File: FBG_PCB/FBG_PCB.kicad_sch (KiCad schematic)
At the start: 36 parts, among them J1 Ground, J10 Pont diviseur Echo In 1-4, J11 17V, J12 17V, J13 Echo Out 5-8, J14 17V, J15 Buck converter 17V/5V, J16 Raspberry Power, J17 ES 5V + 5V, J18 5V, J19 5V, J2 Main switch + ES 17V, J20 5V, J21 5V, J3 Ground, J4 Ground, J5 Ground, J6 Echo Out 1-4, J8 Vin 17V, J9 Pont diviseur Echo In 5-8

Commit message: Lot of new connectors
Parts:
- removed J12, J14: 17V, Connector_Molex:Molex_SL_171971-0004_1x04_P2.54mm_Vertical, symbol Connector:Conn_01x04_Pin
- added J19: switch + ES 12V, Connector_Molex:Molex_SL_171971-0004_1x04_P2.54mm_Vertical, symbol Connector:Conn_01x04_Pin
- added J2: Vin 12V, Connector_JST:JST_NV_B02P-NV_1x02_P5.00mm_Vertical, symbol Connector:Conn_01x02_Pin
- added J20, J21: 12V, Connector_Molex:Molex_SL_171971-0004_1x04_P2.54mm_Vertical, symbol Connector:Conn_01x04_Pin
- added J26: Control Driver Motor In, Connector_Molex:Molex_SL_171971-0004_1x04_P2.54mm_Vertical, symbol Connector:Conn_01x04_Pin
- added J27: Control Driver Motor In +Out, Connector_Molex:Molex_SL_171971-0004_1x04_P2.54mm_Vertical, symbol Connector:Conn_01x04_Pin
- added J28: Control Driver Motor Out, Connector_Molex:Molex_SL_171971-0004_1x04_P2.54mm_Vertical, symbol Connector:Conn_01x04_Pin
- added J29, J30, J31, J8, J9: Ground, Connector_Molex:Molex_SL_171971-0004_1x04_P2.54mm_Vertical, symbol Connector:Conn_01x04_Pin
- J10: renamed from J2; value Main switch + ES 17V -> Raspberry +17V switch
- J11: renamed from J15; value Buck converter 17V/5V -> Buck converter 17V/5V
- J12: renamed from J16; value Raspberry Power -> Raspberry Power+ 5V
- renumbered J8 to J1, J11 to J13, J17 to J14, J18 to J15, J19 to J16, J20 to J17, J21 to J18, J10 to J22, J9 to J23, J6 to J24, J13 to J25, J5 to J4, J1 to J5, J3 to J6, J4 to J7, R11 to R10, R13 to R11, R15 to R12, R10 to R13, R12 to R14, R14 to R15, R7 to R4, R4 to R5, R5 to R6, R6 to R7
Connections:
- net at R4.2, R8.1: now also J24.1 (Pin_1); no longer J24.4 (Pin_4)
- net at R11.2, R15.1: now also J25.2 (Pin_2); no longer J25.3 (Pin_3)
- net at J1.2 (Pin_2), J11.3 (Pin_3), J4.1 (Pin_1)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: now also J2.2 (Pin_2), J8.1 (Pin_1), J8.2 (Pin_2), J8.3 (Pin_3), J8.4 (Pin_4), J9.1 (Pin_1), J9.2 (Pin_2), J9.3 (Pin_3), J9.4 (Pin_4)
- net at J10.4 (Pin_4), J13.1 (Pin_1), J13.2 (Pin_2)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: now also J10.2 (Pin_2), J10.3 (Pin_3), J11.4 (Pin_4)
- net at R3.2, R7.1: now also J24.2 (Pin_2); no longer J24.3 (Pin_3)
- net at R10.2, R14.1: now also J25.3 (Pin_3); no longer J25.2 (Pin_2)
- net at R2.2, R6.1: now also J24.3 (Pin_3); no longer J24.2 (Pin_2)
- net at R12.2, R16.1: now also J25.1 (Pin_1); no longer J25.4 (Pin_4)
- net at R1.2, R5.1: now also J24.4 (Pin_4); no longer J24.1 (Pin_1)
- net at R13.1, R9.2: now also J25.4 (Pin_4); no longer J25.1 (Pin_1)
- new net: J19.1 (Pin_1), J20.1 (Pin_1), J20.2 (Pin_2), J20.3 (Pin_3), J20.4 (Pin_4), J21.1 (Pin_1), J21.2 (Pin_2), J21.3 (Pin_3), J21.4 (Pin_4)
- new net: J19.4 (Pin_4), J2.1 (Pin_1)
- new net: J27.1 (Pin_1), J27.4 (Pin_4)
- new net: J27.2 (Pin_2), J27.3 (Pin_3)
- new net: J26.1 (Pin_1), J28.1 (Pin_1)
- new net: J26.2 (Pin_2), J28.2 (Pin_2)
- new net: J26.3 (Pin_3), J28.3 (Pin_3)
- new net: J26.4 (Pin_4), J28.4 (Pin_4)
- new net: J19.2 (Pin_2), J19.3 (Pin_3)
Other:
- moved on the sheet: J1, J14, J15, J16, J17, J18

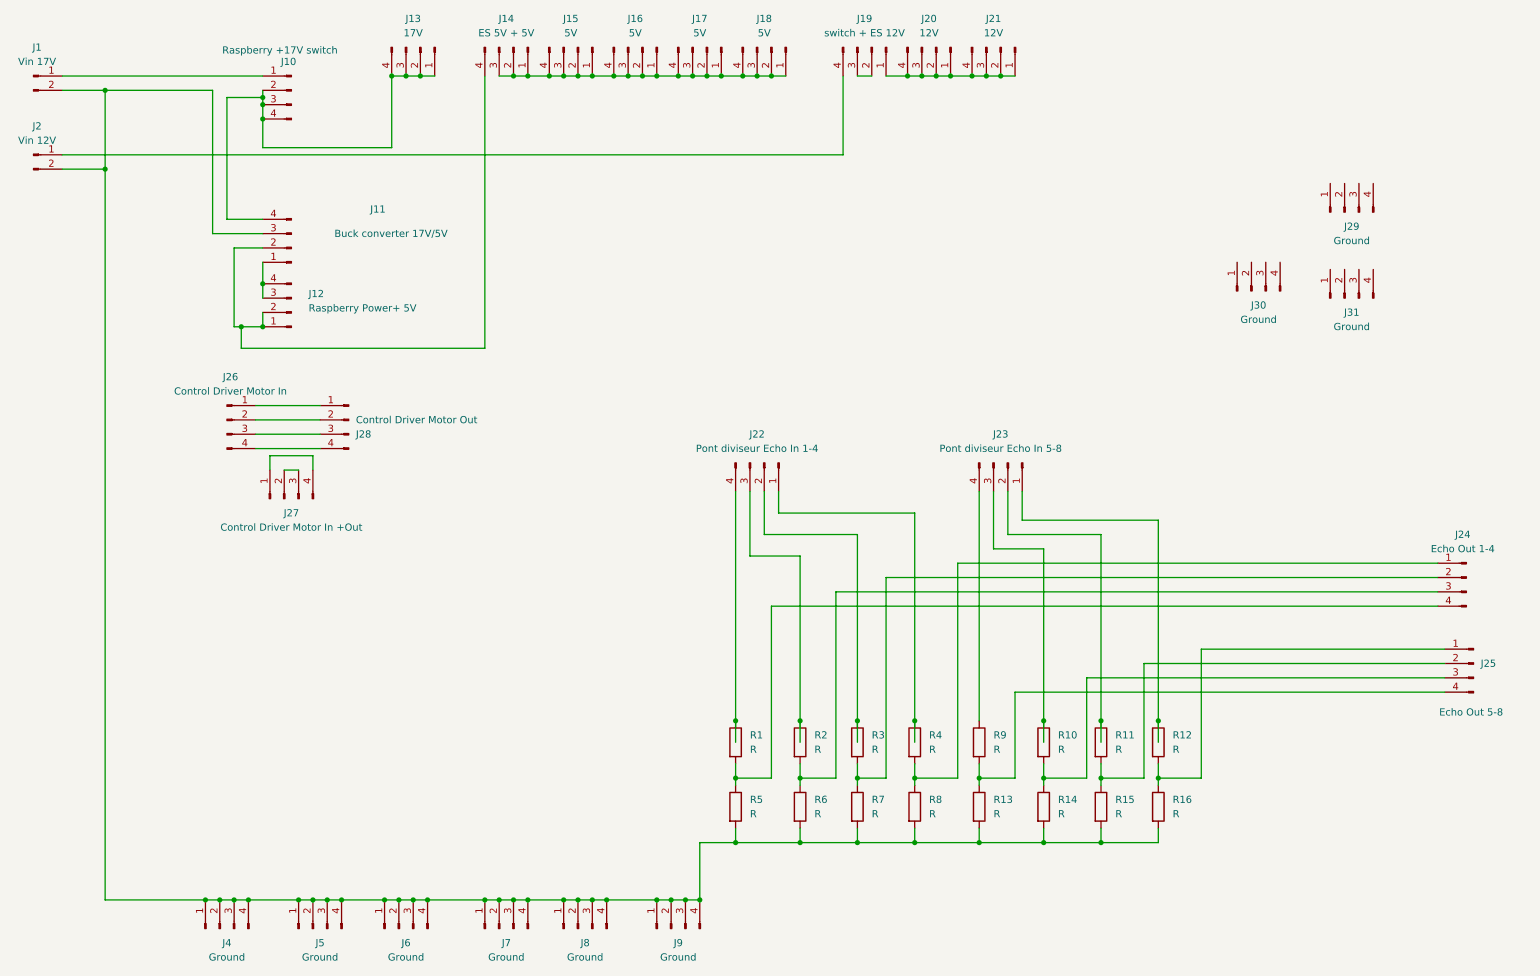
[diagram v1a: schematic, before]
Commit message: trig + echo
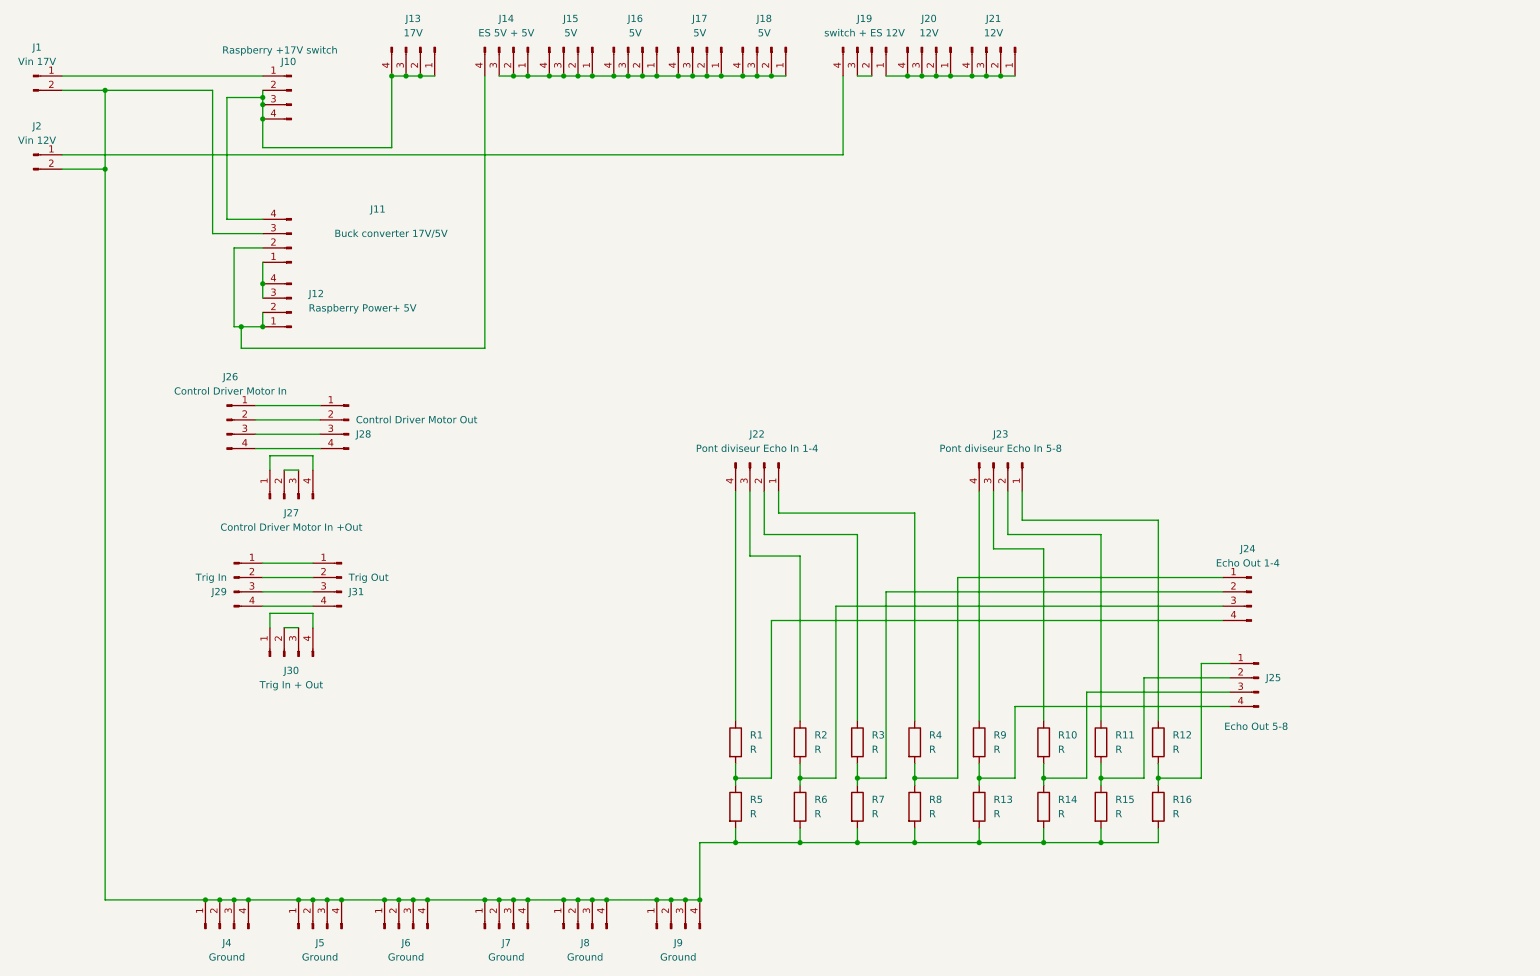
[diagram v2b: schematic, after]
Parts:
- J29: value Ground -> Trig In
- J30: value Ground -> Trig In + Out
- J31: value Ground -> Trig Out
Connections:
- net at J29.1 (Pin_1): now also J31.1 (Pin_1)
- net at J29.2 (Pin_2): now also J31.2 (Pin_2)
- net at J29.3 (Pin_3): now also J31.3 (Pin_3)
- net at J29.4 (Pin_4): now also J31.4 (Pin_4)
- net at J30.1 (Pin_1): now also J30.4 (Pin_4)
- net at J30.2 (Pin_2): now also J30.3 (Pin_3)
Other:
- moved on the sheet: J24, J25, J29, J30, J31

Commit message: V1
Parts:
- added J32: I2C Out, Connector_Molex:Molex_SL_171971-0004_1x04_P2.54mm_Vertical, symbol Connector:Conn_01x04_Pin
- added J33: I2C SCL In, Connector_Molex:Molex_SL_171971-0004_1x04_P2.54mm_Vertical, symbol Connector:Conn_01x04_Pin
- added J34: I2C SCL In +SDA In, Connector_Molex:Molex_SL_171971-0004_1x04_P2.54mm_Vertical, symbol Connector:Conn_01x04_Pin
- added J35: I2C SDA In, Connector_Molex:Molex_SL_171971-0004_1x04_P2.54mm_Vertical, symbol Connector:Conn_01x04_Pin
- added J36: Control Motor CanLift Out +In, Connector_Molex:Molex_SL_171971-0004_1x04_P2.54mm_Vertical, symbol Connector:Conn_01x04_Pin
- added J37: Encoder M1 +M2 Out, Connector_Molex:Molex_SL_171971-0004_1x04_P2.54mm_Vertical, symbol Connector:Conn_01x04_Pin
- added J38: Encoder M1 +M2 In, Connector_Molex:Molex_SL_171971-0004_1x04_P2.54mm_Vertical, symbol Connector:Conn_01x04_Pin
- added J39, J41: Bonus Out, Connector_Molex:Molex_SL_171971-0004_1x04_P2.54mm_Vertical, symbol Connector:Conn_01x04_Pin
- added J40, J42: Bonus In, Connector_Molex:Molex_SL_171971-0004_1x04_P2.54mm_Vertical, symbol Connector:Conn_01x04_Pin
- J22: value Pont diviseur Echo In 1-4 -> Pont diviseur Echo Out 1-4
- J23: value Pont diviseur Echo In 5-8 -> Pont diviseur Echo Out 5-8
- J24: value Echo Out 1-4 -> Echo In 1-4
- J25: value Echo Out 5-8 -> Echo In 5-8
- J26: value Control Driver Motor In -> Control Driver Motor Out
- J27: value Control Driver Motor In +Out -> Control Driver Motor Out + Trig Out
- J28: value Control Driver Motor Out -> Control Driver Motor In
- J30: value Trig In + Out -> Control Driver Motor In + Trig In
- R1, R10, R11, R12, R13, R14, R15, R16, R2, R3, R4, R5, R6, R7, R8, R9: footprint Resistor_THT:R_Axial_DIN0411_L9.9mm_D3.6mm_P25.40mm_Horizontal -> Resistor_THT:R_Axial_DIN0207_L6.3mm_D2.5mm_P10.16mm_Horizontal
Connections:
- net at J22.1 (Pin_1): now also R1.1; no longer R4.1
- net at R4.2, R8.1: now also J24.4 (Pin_4); no longer J24.1 (Pin_1)
- net at J1.2 (Pin_2), J2.2 (Pin_2), J4.1 (Pin_1)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: now also J11.2 (Pin_2); no longer J11.3 (Pin_3)
- net at R11.2, R15.1: now also J25.3 (Pin_3); no longer J25.2 (Pin_2)
- net at J22.2 (Pin_2): now also R2.1; no longer R3.1
- net at J22.3 (Pin_3): now also R3.1; no longer R2.1
- net at J22.4 (Pin_4): now also R4.1; no longer R1.1
- net at R3.2, R7.1: now also J24.3 (Pin_3); no longer J24.2 (Pin_2)
- net at R10.2, R14.1: now also J25.2 (Pin_2); no longer J25.3 (Pin_3)
- net at J30.1 (Pin_1): now also J27.1 (Pin_1); no longer J30.4 (Pin_4)
- net at J30.2 (Pin_2): now also J27.2 (Pin_2); no longer J30.3 (Pin_3)
- net at R2.2, R6.1: now also J24.2 (Pin_2); no longer J24.3 (Pin_3)
- net at J23.3 (Pin_3): now also R11.1; no longer R10.1
- net at J23.2 (Pin_2): now also R10.1; no longer R11.1
- net at J10.2 (Pin_2), J10.3 (Pin_3), J10.4 (Pin_4)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: now also J11.1 (Pin_1); no longer J11.4 (Pin_4)
- net at J27.4 (Pin_4): now also J30.4 (Pin_4); no longer J27.1 (Pin_1)
- net at J27.3 (Pin_3): now also J30.3 (Pin_3); no longer J27.2 (Pin_2)
- net at R12.1: now also J23.4 (Pin_4); no longer J23.1 (Pin_1)
- net at R12.2, R16.1: now also J25.4 (Pin_4); no longer J25.1 (Pin_1)
- net at R1.2, R5.1: now also J24.1 (Pin_1); no longer J24.4 (Pin_4)
- net at J12.1 (Pin_1), J12.2 (Pin_2), J14.4 (Pin_4): now also J11.3 (Pin_3); no longer J11.2 (Pin_2)
- net at J12.3 (Pin_3), J12.4 (Pin_4): now also J11.4 (Pin_4); no longer J11.1 (Pin_1)
- net at R9.1: now also J23.1 (Pin_1); no longer J23.4 (Pin_4)
- net at R13.1, R9.2: now also J25.1 (Pin_1); no longer J25.4 (Pin_4)
- new net: J32.1 (Pin_1), J32.2 (Pin_2), J33.1 (Pin_1), J33.2 (Pin_2), J33.3 (Pin_3), J33.4 (Pin_4), J34.1 (Pin_1), J34.2 (Pin_2)
- new net: J39.1 (Pin_1), J40.1 (Pin_1)
- new net: J39.2 (Pin_2), J40.2 (Pin_2)
- new net: J39.3 (Pin_3), J40.3 (Pin_3)
- new net: J39.4 (Pin_4), J40.4 (Pin_4)
- new net: J32.3 (Pin_3), J32.4 (Pin_4), J34.3 (Pin_3), J34.4 (Pin_4), J35.1 (Pin_1), J35.2 (Pin_2), J35.3 (Pin_3), J35.4 (Pin_4)
- new net: J37.1 (Pin_1), J38.1 (Pin_1)
- new net: J37.2 (Pin_2), J38.2 (Pin_2)
- new net: J37.3 (Pin_3), J38.3 (Pin_3)
- new net: J37.4 (Pin_4), J38.4 (Pin_4)
- new net: J36.1 (Pin_1), J36.3 (Pin_3)
- new net: J36.2 (Pin_2), J36.4 (Pin_4)
- new net: J41.1 (Pin_1), J42.1 (Pin_1)
- new net: J41.2 (Pin_2), J42.2 (Pin_2)
- new net: J41.3 (Pin_3), J42.3 (Pin_3)
- new net: J41.4 (Pin_4), J42.4 (Pin_4)
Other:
- moved on the sheet: J11, J26, J27, J28, J29, J30, J31

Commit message: V2.1
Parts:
- J22: value Pont diviseur Echo Out 1-4 -> Echo Out 1-4
- J23: value Pont diviseur Echo Out 5-8 -> Echo Out 5-8
- J26: value Control Driver Motor Out -> Driver Motor Out
- J27: value Control Driver Motor Out + Trig Out -> Driver Motor Out + Trig Out
- J28: value Control Driver Motor In -> Driver Motor In
- J30: value Control Driver Motor In + Trig In -> Driver Motor In + Trig In
- J36: value Control Motor CanLift Out +In -> Motor CanLift Out +In
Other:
- company: (none) -> Noteris Corporation
- title: (none) -> PCB Board Eurobot FBG Team
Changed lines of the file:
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@@
 	(generator_version "9.0")
 	(paper "A4")
+	(title_block
+		(title "PCB Board Eurobot FBG Team")
+		(date "16/03/2025")
+		(rev "1.0")
+		(company "Noteris Corporation")
+	)
 	(junction
 		(at 109.22 25.4)
@@
 			)
 		)
-		(property "Value" "Pont diviseur Echo Out 1-4"
+		(property "Value" "Echo Out 1-4"
 			(at 146.05 91.44 90)
 			(effects
@@
 			)
 		)
-		(property "Value" "Control Driver Motor In + Trig In"
-			(at 108.204 104.648 0)
+		(property "Value" "Driver Motor In + Trig In"
+			(at 102.87 104.394 0)
 			(effects
 				(font
@@
 			)
 		)
-		(property "Value" "Control Driver Motor Out + Trig Out"
+		(property "Value" "Driver Motor Out + Trig Out"
 			(at 51.054 105.156 0)
 			(effects
@@
 			)
 		)
-		(property "Value" "Control Driver Motor Out"
+		(property "Value" "Driver Motor Out"
 			(at 52.578 93.218 0)
 			(effects
@@
 			)
 		)
-		(property "Value" "Control Motor CanLift Out +In"
+		(property "Value" "Motor CanLift Out +In"
 			(at 114.554 59.69 0)
 			(effects
@@
 			)
 		)
-		(property "Value" "Control Driver Motor In"
+		(property "Value" "Driver Motor In"
 			(at 91.44 91.4401 0)
 			(effects
@@
 			)
 		)
-		(property "Value" "Pont diviseur Echo Out 5-8"
+		(property "Value" "Echo Out 5-8"
 			(at 189.23 91.44 90)
 			(effects
